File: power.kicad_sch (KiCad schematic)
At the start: 10 parts, among them U1 TPS63802DLAR

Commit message: Moved 5v boost to the boost schematic
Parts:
- removed 5V: TestPoint, TestPoint:TestPoint_Pad_2.0x2.0mm, symbol Connector:TestPoint
- removed BT1: 1.5V, Battery:BatteryHolder_Keystone_2460_1xAA, symbol Device:Battery_Cell
- removed C1: 10uF, Capacitor_SMD:C_0805_2012Metric_Pad1.18x1.45mm_HandSolder, symbol Device:C
- removed C2, C3: 22uF, Capacitor_SMD:C_0805_2012Metric_Pad1.18x1.45mm_HandSolder, symbol Device:C
- removed L1: 470nH, Inductor_SMD:L_Coilcraft_XxL4020, symbol Device:L
- removed R1: 100K, Resistor_SMD:R_0805_2012Metric_Pad1.20x1.40mm_HandSolder, symbol Device:R_US
- removed R2: 806K, Resistor_SMD:R_0805_2012Metric_Pad1.20x1.40mm_HandSolder, symbol Device:R_US
- removed R3: 91K, Resistor_SMD:R_0805_2012Metric_Pad1.20x1.40mm_HandSolder, symbol Device:R_US
- removed U1: TPS63802DLAR, TPS63802DLAR:DLA0010A, symbol TPS63802DLAR:TPS63802DLAR

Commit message: Added HV schematic
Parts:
- added C1: 22u, symbol Device:C_Polarized
- added C2: 1u, symbol Device:C
- added C3: 100u, symbol Device:C_Polarized
- added C4: .1u, symbol Device:C
- added C5: .47u, symbol Device:C
- added D1: US1G, Diode_SMD:D_SMA, symbol Diode:US1G
- added L1: 1u, symbol Device:L_Coupled
- added R1: 40k, symbol Device:R_US
- added R12: 307k, symbol Device:R_US
- added R13: 43k, symbol Device:R_US
- added R2, R3: 4.7k, symbol Device:R_US
- added R4: 2k, symbol Device:R_US
- added R5: 10k, symbol Device:R_US
- added TP1: TestPoint, symbol Connector:TestPoint
- added U2: DS4432, FES_Footprints:21-0036_U8&plus_1_MXM, symbol FES_SymbolLib:ds4432u+
- added U3: LM2586S, TS7B, symbol FES_SymbolLib:LM2586S-5.0_NOPB
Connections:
- new net: R12.2, R13.1, U2.7 (OUT1), U3.3 (FB)
- new net: D1.2 (A), L1.1
- new net: R1.1, U2.3 (FS1)
- new net: R4.1, U3.2 (COMP)
- new net: C5.1, R4.2
- new net: L1.5, L1.6 (1), U3.5 (SW)
- new net 3V3: R2.1, R3.1
- new net ESP32_SCL: R2.2, U2.2 (SCL)
- new net ESP32_SDA: R3.2, U2.1 (SDA)
- new net GND: C1.2, C2.2, C3.2, C4.2, C5.2, L1.8, R1.2, R13.2, R5.2, U2.4 (GND), U3.1 (~ON/OFF), U3.4 (GND), U3.8 (TAB)
- new net HV_OUT: C1.1, C3.1, D1.1 (K), R12.1, R5.1, TP1.1
- new net VCC: C2.1, C4.1, L1.2 (4), L1.3, U2.8 (VCC), U3.7 (VIN)
- no-connect marks 0 -> 2
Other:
- note added: "10u"
- note added: "1m"
- note added: "750032050"

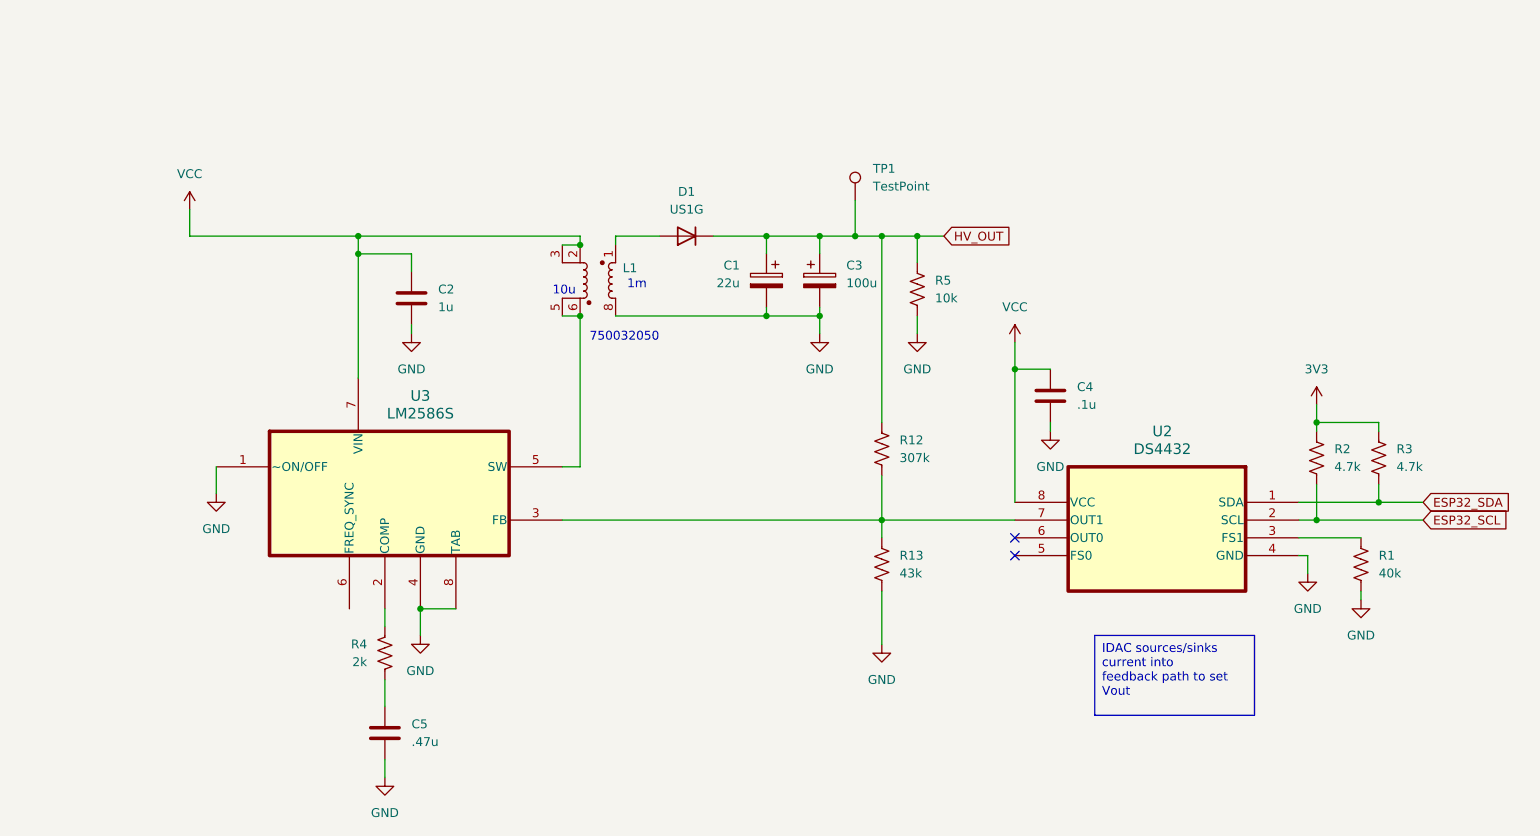
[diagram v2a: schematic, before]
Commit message: changed transformer, feedback resistors
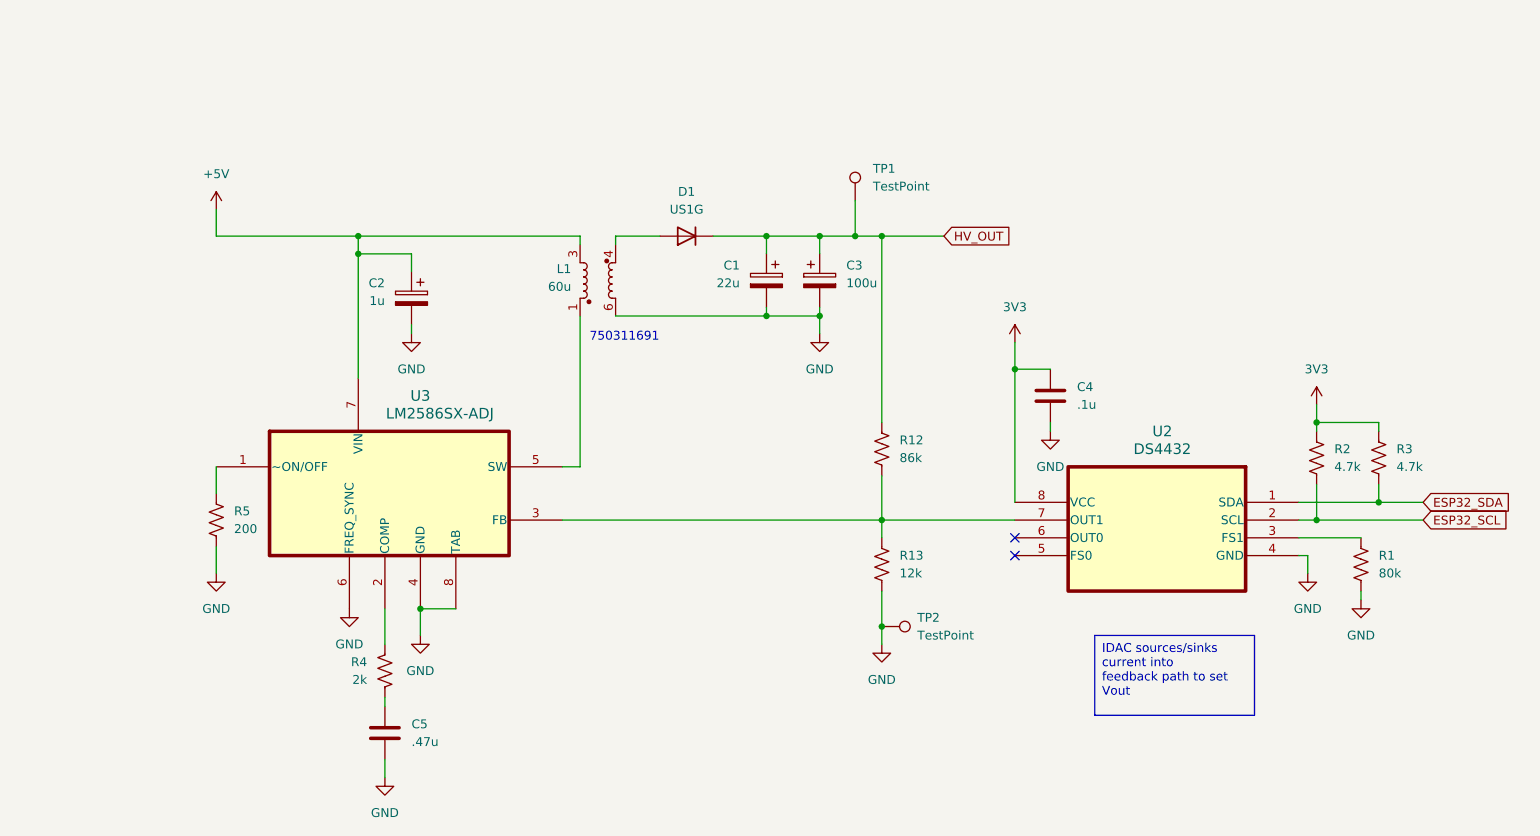
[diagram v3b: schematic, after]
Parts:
- removed C2: 1u, symbol Device:C
- added C2: 1u, symbol Device:C_Polarized
- added TP2: TestPoint, symbol Connector:TestPoint
- L1: value 1u -> 60u
- R1: value 40k -> 80k
- R12: value 307k -> 86k
- R13: value 43k -> 12k
- R5: value 10k -> 200
- U3: value LM2586S -> LM2586SX-ADJ
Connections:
- net 3V3: now also C4.1, U2.8 (VCC)
- net GND: now also L1.6, U3.6 (FREQ_SYNC), C2.2, TP2.1; no longer L1.8, U3.1 (~ON/OFF)
- net HV_OUT: no longer R5.1
- net at D1.2 (A): now also L1.4; no longer L1.1
- removed net VCC: C4.1, L1.2 (4), L1.3, U2.8 (VCC), U3.7 (VIN)
- new net: L1.1, U3.5 (SW)
- new net: R5.1, U3.1 (~ON/OFF)
- new net +5V: C2.1, L1.3, U3.7 (VIN)
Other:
- note added: "750311691"
- note removed: "10u"
- note removed: "1m"
- note removed: "750032050"
- moved on the sheet: R4

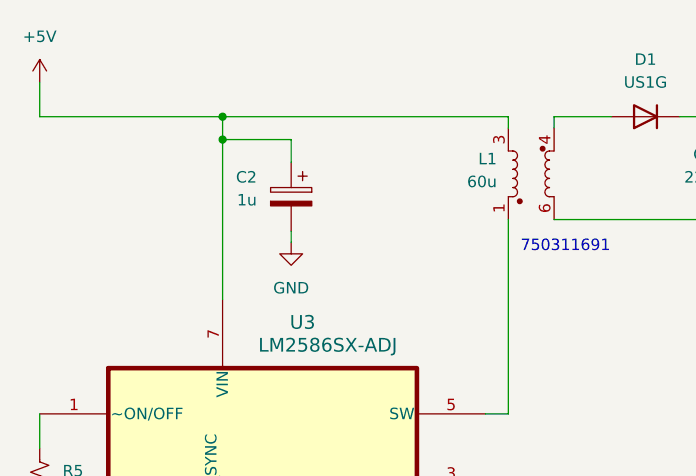
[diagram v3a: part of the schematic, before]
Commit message: Added H-Bridge, completed HV schematic
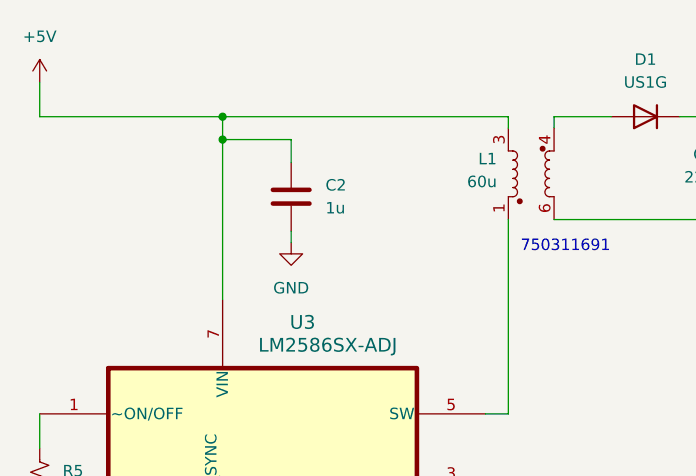
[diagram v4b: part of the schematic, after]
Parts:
- removed C2: 1u, symbol Device:C_Polarized
- added C2: 1u, symbol Device:C
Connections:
- net +5V: now also C2.1
- net GND: now also C2.2
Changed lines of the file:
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@@
-	)
-	(symbol
-		(lib_id "Device:C_Polarized")
-		(at 90.17 73.66 0)
-		(mirror y)
-		(unit 1)
-		(exclude_from_sim no)
-		(in_bom yes)
-		(on_board yes)
-		(dnp no)
-		(property "Reference" "C2"
-			(at 86.36 71.5009 0)
-			(effects
-				(font
-					(size 1.27 1.27)
-				)
-				(justify left)
-			)
-		)
-		(property "Value" "1u"
-			(at 86.36 74.0409 0)
-			(effects
-				(font
-					(size 1.27 1.27)
-				)
-				(justify left)
-			)
-		)
-		(property "Footprint" ""
-			(at 89.2048 77.47 0)
-			(effects
-				(font
-					(size 1.27 1.27)
-				)
-				(hide yes)
-			)
-		)
-		(property "Datasheet" "~"
-			(at 90.17 73.66 0)
-			(effects
-				(font
-					(size 1.27 1.27)
-				)
-				(hide yes)
-			)
-		)
-		(property "Description" "Polarized capacitor"
-			(at 90.17 73.66 0)
-			(effects
-				(font
-					(size 1.27 1.27)
-				)
-				(hide yes)
-			)
-		)
-		(pin "1"
-		)
-		(pin "2"
-		)
-		(instances
-			(project "FES_Hardware"
-				(path "/225cfa82-97e7-4320-90e1-4d94ef39f9f2/9d03af3c-7e27-487a-be84-d59389aa1574"
-					(reference "C2")
-					(unit 1)
-				)
-			)
-		)
 	)
 	(symbol
@@
 					(unit 1)
 				)
+			)
+		)
+	)
+	(symbol
+		(lib_id "Device:C")
+		(at 90.17 73.66 0)
+		(unit 1)
+		(exclude_from_sim no)
+		(in_bom yes)
+		(on_board yes)
+		(dnp no)
+		(fields_autoplaced yes)
+		(property "Reference" "C2"
+			(at 93.98 72.3899 0)
+			(effects
+				(font
+					(size 1.27 1.27)
+				)
+				(justify left)
+			)
+		)
+		(property "Value" "1u"
+			(at 93.98 74.9299 0)
+			(effects
+				(font
+					(size 1.27 1.27)
+				)
+				(justify left)
+			)
+		)
+		(property "Footprint" ""
+			(at 91.1352 77.47 0)
+			(effects
+				(font
+					(size 1.27 1.27)
+				)
+				(hide yes)
+			)
+		)
+		(property "Datasheet" "~"
+			(at 90.17 73.66 0)
+			(effects
+				(font
+					(size 1.27 1.27)
+				)
+				(hide yes)
+			)
+		)
+		(property "Description" "Unpolarized capacitor"
+			(at 90.17 73.66 0)
+			(effects
+				(font
+					(size 1.27 1.27)
+				)
+				(hide yes)
+			)
+		)
+		(pin "2"
+		)
+		(pin "1"
+		)
+		(instances
+			(project ""
+				(path "/225cfa82-97e7-4320-90e1-4d94ef39f9f2/9d03af3c-7e27-487a-be84-d59389aa1574"
+					(reference "C2")
+					(unit 1)
+				)

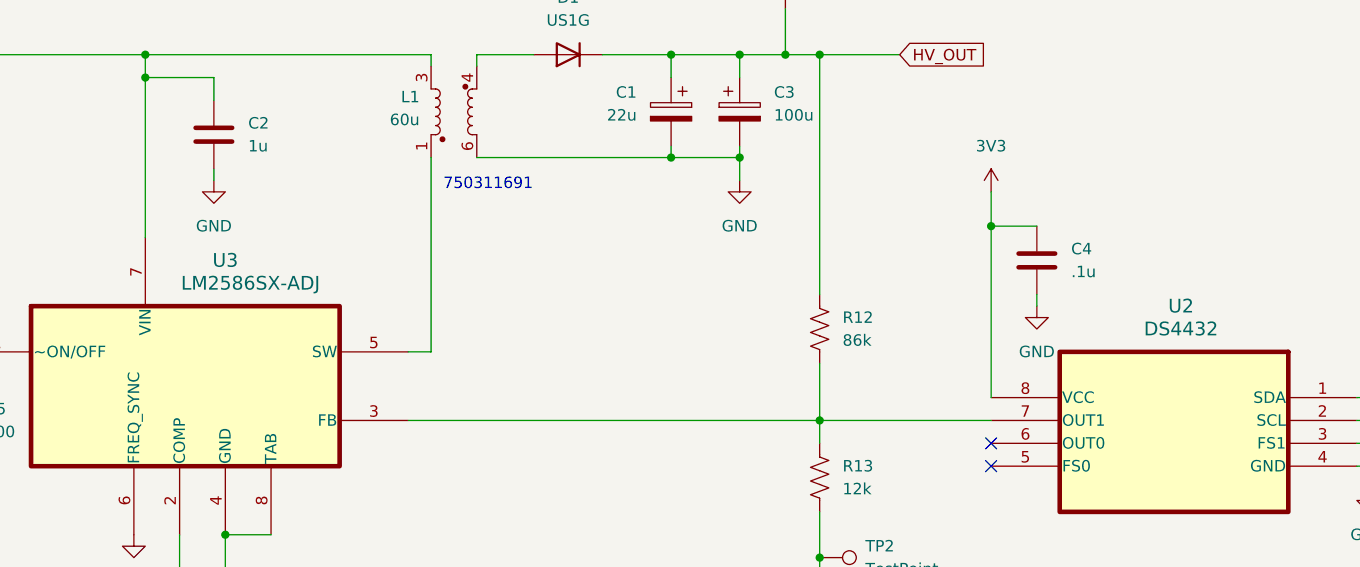
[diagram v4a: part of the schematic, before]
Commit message: updated symbols background to be transparent
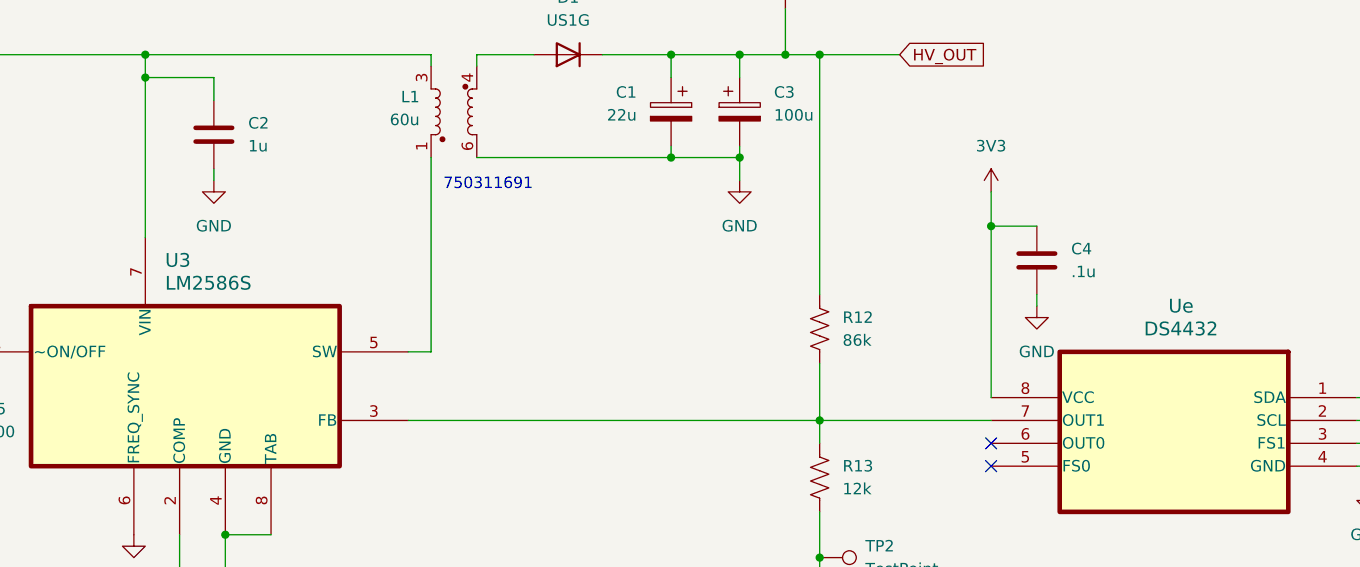
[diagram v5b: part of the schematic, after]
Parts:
- U3: value LM2586SX-ADJ -> LM2586S
- Ue: renamed from U2; footprint FES_Footprints:21-0036_U8&plus_1_MXM -> 21-0036_U8+1_MXM
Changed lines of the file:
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@@
 		(on_board yes)
 		(dnp no)
-		(property "Reference" "U2"
+		(property "Reference" "Ue"
 			(at 197.6311 92.71 0)
 			(effects
@@
 			)
 		)
-		(property "Footprint" "FES_Footprints:21-0036_U8&plus_1_MXM"
+		(property "Footprint" "21-0036_U8+1_MXM"
 			(at 217.17 102.87 0)
 			(effects
@@
 			(project ""
 				(path "/225cfa82-97e7-4320-90e1-4d94ef39f9f2/9d03af3c-7e27-487a-be84-d59389aa1574"
-					(reference "U2")
+					(reference "Ue")
 					(unit 1)
 				)
@@
 	)
 	(symbol
+		(lib_id "FES_SymbolLib:LM2586S-5.0_NOPB")
+		(at 41.91 97.79 0)
+		(unit 1)
+		(exclude_from_sim no)
+		(in_bom yes)
+		(on_board yes)
+		(dnp no)
+		(fields_autoplaced yes)
+		(property "Reference" "U3"
+			(at 84.7441 87.63 0)
+			(effects
+				(font
+					(size 1.524 1.524)
+				)
+				(justify left)
+			)
+		)
+		(property "Value" "LM2586S"
+			(at 84.7441 90.17 0)
+			(effects
+				(font
+					(size 1.524 1.524)
+				)
+				(justify left)
+			)
+		)
+		(property "Footprint" "TS7B"
+			(at 62.23 97.79 0)
+			(effects
+				(font
+					(size 1.27 1.27)
+					(italic yes)
+				)
+				(hide yes)
+			)
+		)
+		(property "Datasheet" "LM2586S-5.0/NOPB"
+			(at 62.23 97.79 0)
+			(effects
+				(font
+					(size 1.27 1.27)
+					(italic yes)
+				)
+				(hide yes)
+			)
+		)
+		(property "Description" ""
+			(at 62.23 97.79 0)
+			(effects
+				(font
+					(size 1.27 1.27)
+				)
+				(hide yes)
+			)
+		)
+		(pin "8"
+		)
+		(pin "2"
+		)
+		(pin "3"
+		)
+		(pin "4"
+		)
+		(pin "1"
+		)
+		(pin "6"
+		)
+		(pin "7"
+		)
+		(pin "5"
+		)
+		(instances
+			(project ""
+				(path "/225cfa82-97e7-4320-90e1-4d94ef39f9f2/9d03af3c-7e27-487a-be84-d59389aa1574"
+					(reference "U3")
+					(unit 1)
+				)
+			)
+		)
+	)
+	(symbol
 		(lib_id "power:GND")
 		(at 148.59 78.74 0)
@@
 					(unit 1)
 				)
-			)
-		)
-	)
-	(symbol
-		(lib_id "FES_SymbolLib:LM2586S-5.0_NOPB")
-		(at 41.91 97.79 0)
-		(unit 1)
-		(exclude_from_sim no)
-		(in_bom yes)
-		(on_board yes)
-		(dnp no)
-		(property "Reference" "U3"
-			(at 91.44 87.63 0)
-			(effects
-				(font
-					(size 1.524 1.524)
-				)
-			)
-		)
-		(property "Value" "LM2586SX-ADJ"
-			(at 94.234 90.17 0)
-			(effects
-				(font
-					(size 1.524 1.524)
-				)
-			)
-		)
-		(property "Footprint" "TS7B"
-			(at 62.23 97.79 0)
-			(effects
-				(font
-					(size 1.27 1.27)
-					(italic yes)
-				)
-				(hide yes)
-			)
-		)
-		(property "Datasheet" "LM2586S-5.0/NOPB"
-			(at 62.23 97.79 0)
-			(effects
-				(font
-					(size 1.27 1.27)
-					(italic yes)
-				)
-				(hide yes)
-			)
-		)
-		(property "Description" ""
-			(at 62.23 97.79 0)
-			(effects
-				(font
-					(size 1.27 1.27)
-				)
-				(hide yes)
-			)
-		)
-		(pin "6"
-		)
-		(pin "2"
-		)
-		(pin "4"
-		)
-		(pin "1"
-		)
-		(pin "5"
-		)
-		(pin "3"
-		)
-		(pin "7"
-		)
-		(pin "8"
-		)
-		(instances
-			(project ""
-				(path "/225cfa82-97e7-4320-90e1-4d94ef39f9f2/9d03af3c-7e27-487a-be84-d59389aa1574"
-					(reference "U3")
-					(unit 1)
-				)
